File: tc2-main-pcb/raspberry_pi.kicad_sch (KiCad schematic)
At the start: 30 parts, among them J1 Screw_Terminal_01x01, J2 Screw_Terminal_01x01, J4 Raspberry_Pi_2_3, J5 Screw_Terminal_01x01, J6 Screw_Terminal_01x01, J8 Screw_Terminal_01x01, U14 MAX98357AEWL+T, U15 74HC4052, U18 TCA4311ADGKR

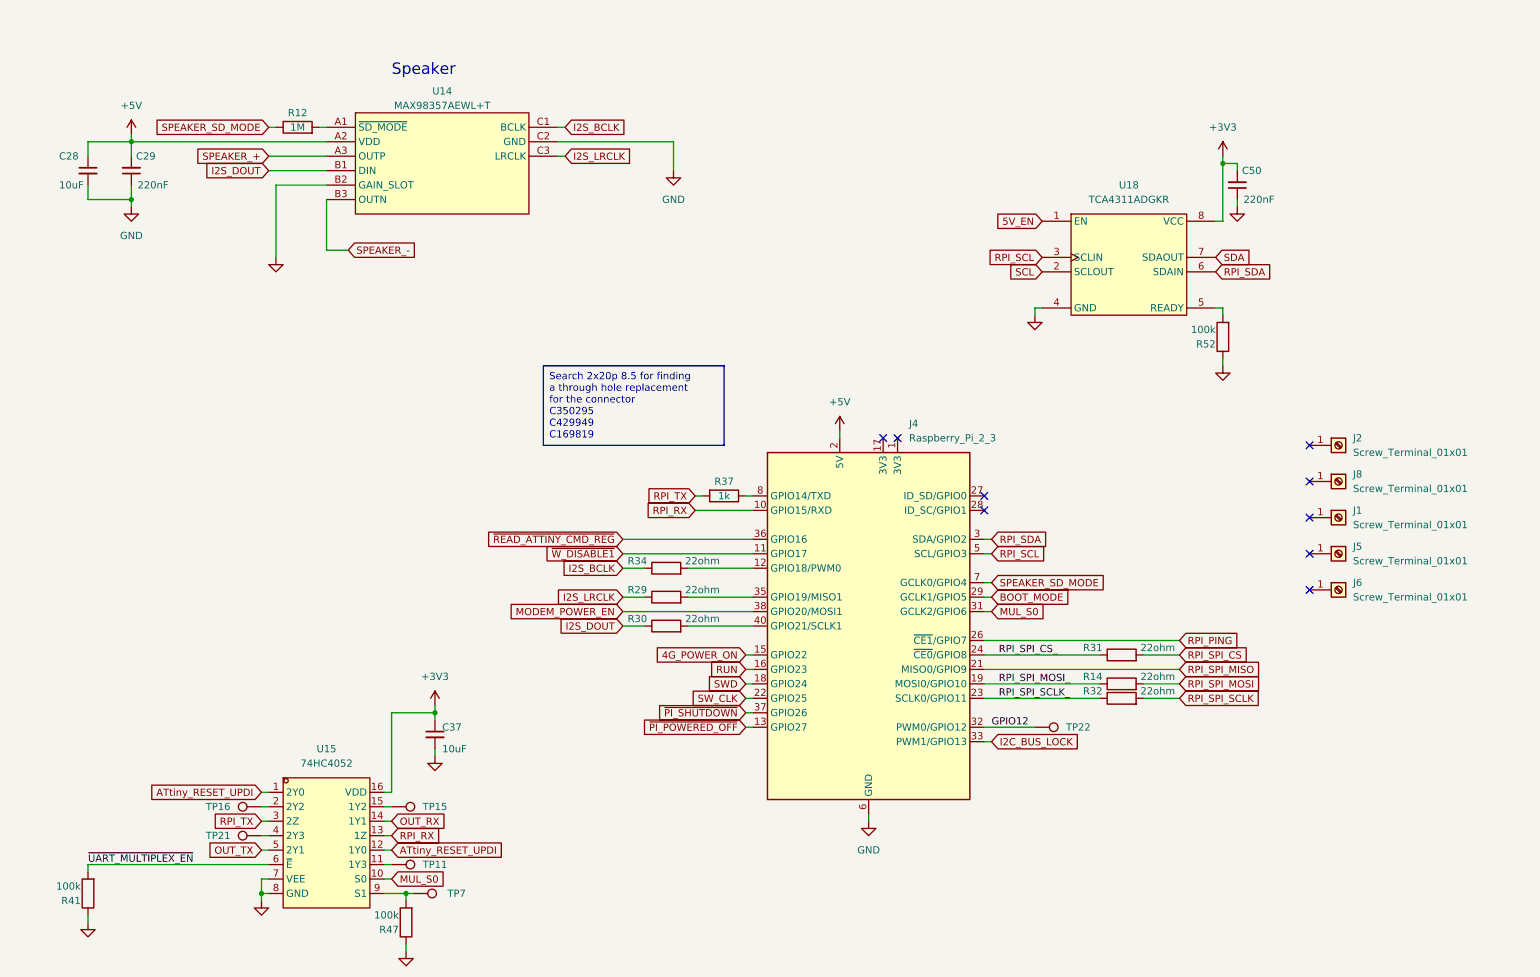
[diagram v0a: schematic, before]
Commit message: Update to use touch sensor
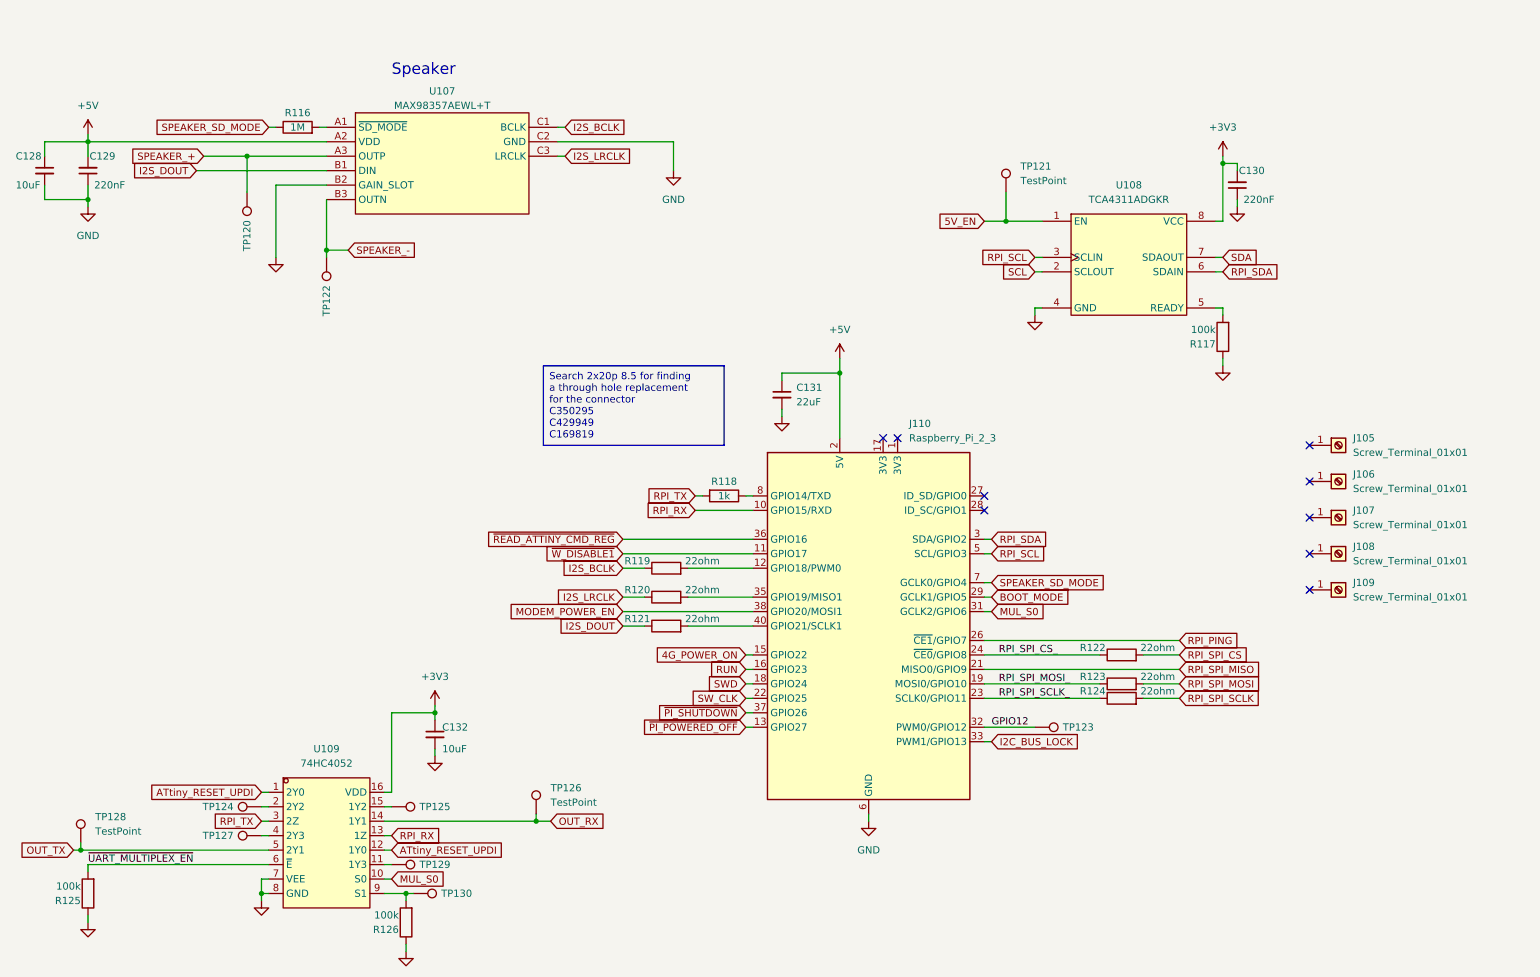
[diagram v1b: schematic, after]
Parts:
- added C131: 22uF, Capacitor_SMD:C_0603_1608Metric, symbol Device:C_Small
- added TP120, TP122: TestPoint, cacophony-library:TP, symbol Connector:TestPoint
- added TP121, TP126, TP128: TestPoint, TestPoint:TestPoint_Pad_D1.0mm, symbol Connector:TestPoint
- J110: renamed from J4; footprint cacophony-library:HDR-SMD_40P-P2.54-V-F-R2-C20-LS8.2-EH -> cacophony-library:rpi-throughhole-socket; LCSC C2685098 -> C350295
- R116: renamed from R12; LCSC C22935 -> C326730
- renumbered C28 to C128, C29 to C129, C50 to C130, C37 to C132, J2 to J105, J8 to J106, J1 to J107, J5 to J108, J6 to J109, R52 to R117, R37 to R118, R34 to R119, R29 to R120, R30 to R121, R31 to R122, R14 to R123, R32 to R124, R41 to R125, R47 to R126, TP22 to TP123, TP16 to TP124, TP15 to TP125, TP21 to TP127, TP11 to TP129, TP7 to TP130, U14 to U107, U18 to U108, U15 to U109
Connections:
- net +5V: now also C131.1
- net 5V_EN: now also TP121.1
- net GND: now also C131.2
- net OUT_RX: now also TP126.1
- net OUT_TX: now also TP128.1
- net SPEAKER_+: now also TP120.1
- net SPEAKER_-: now also TP122.1
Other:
- moved on the sheet: C128, C129

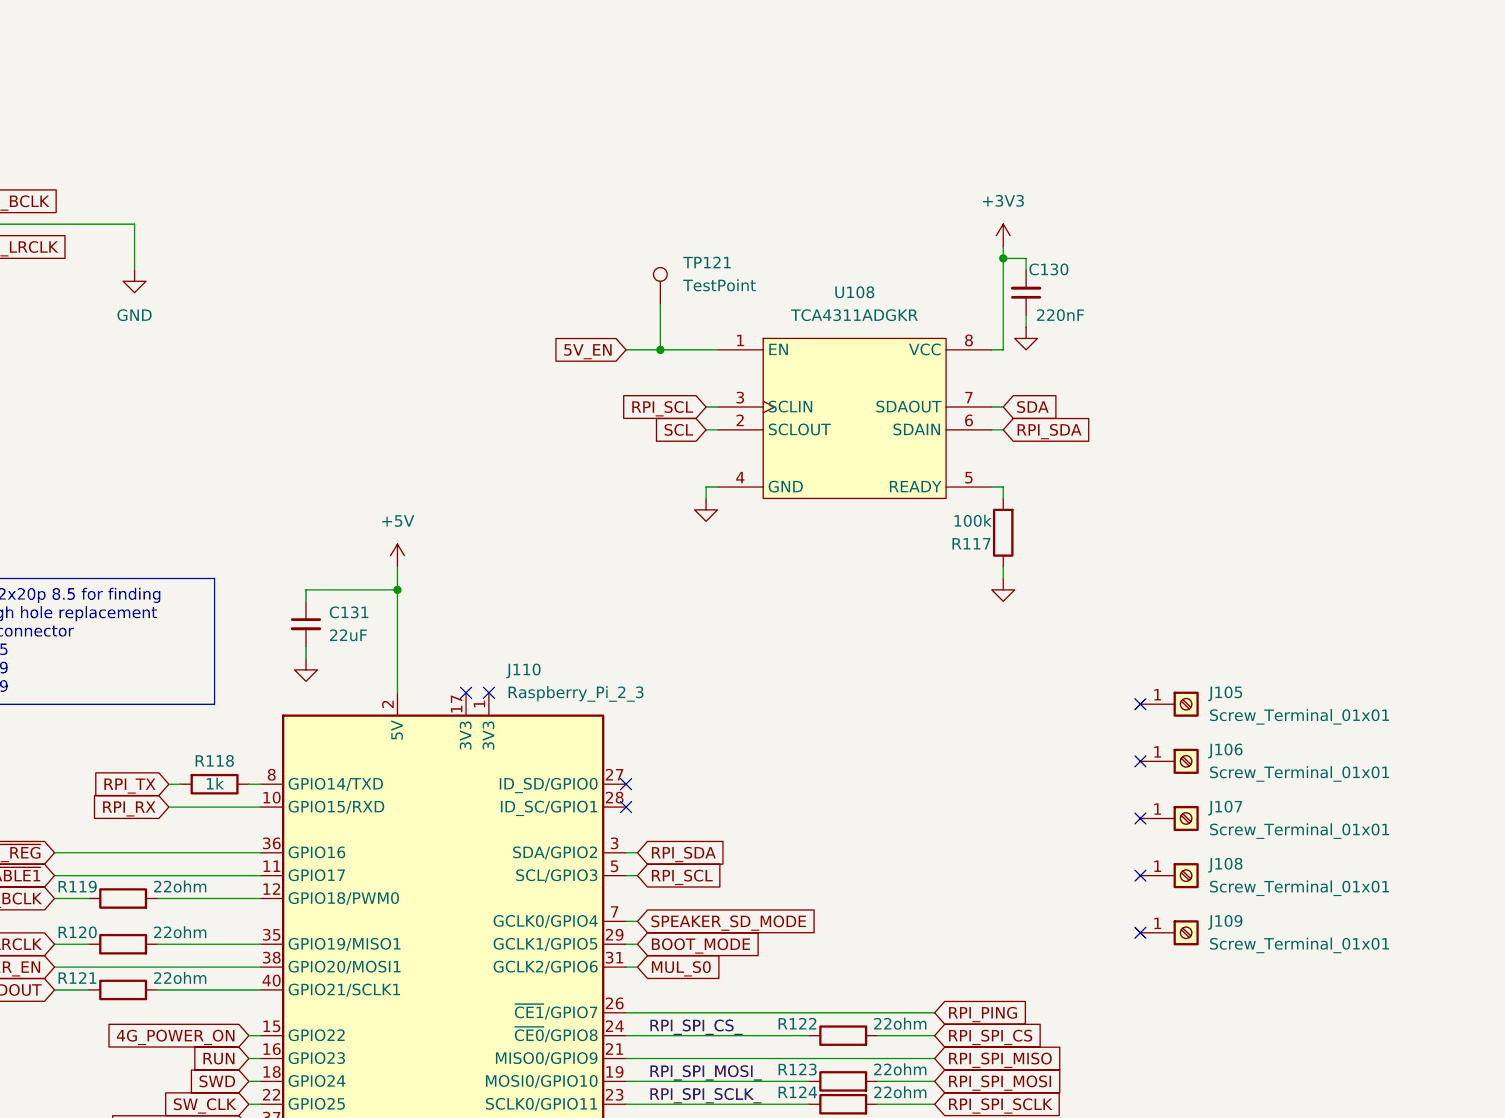
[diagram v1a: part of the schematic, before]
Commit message: Change to through hole connector and add simcard PCB to pannel
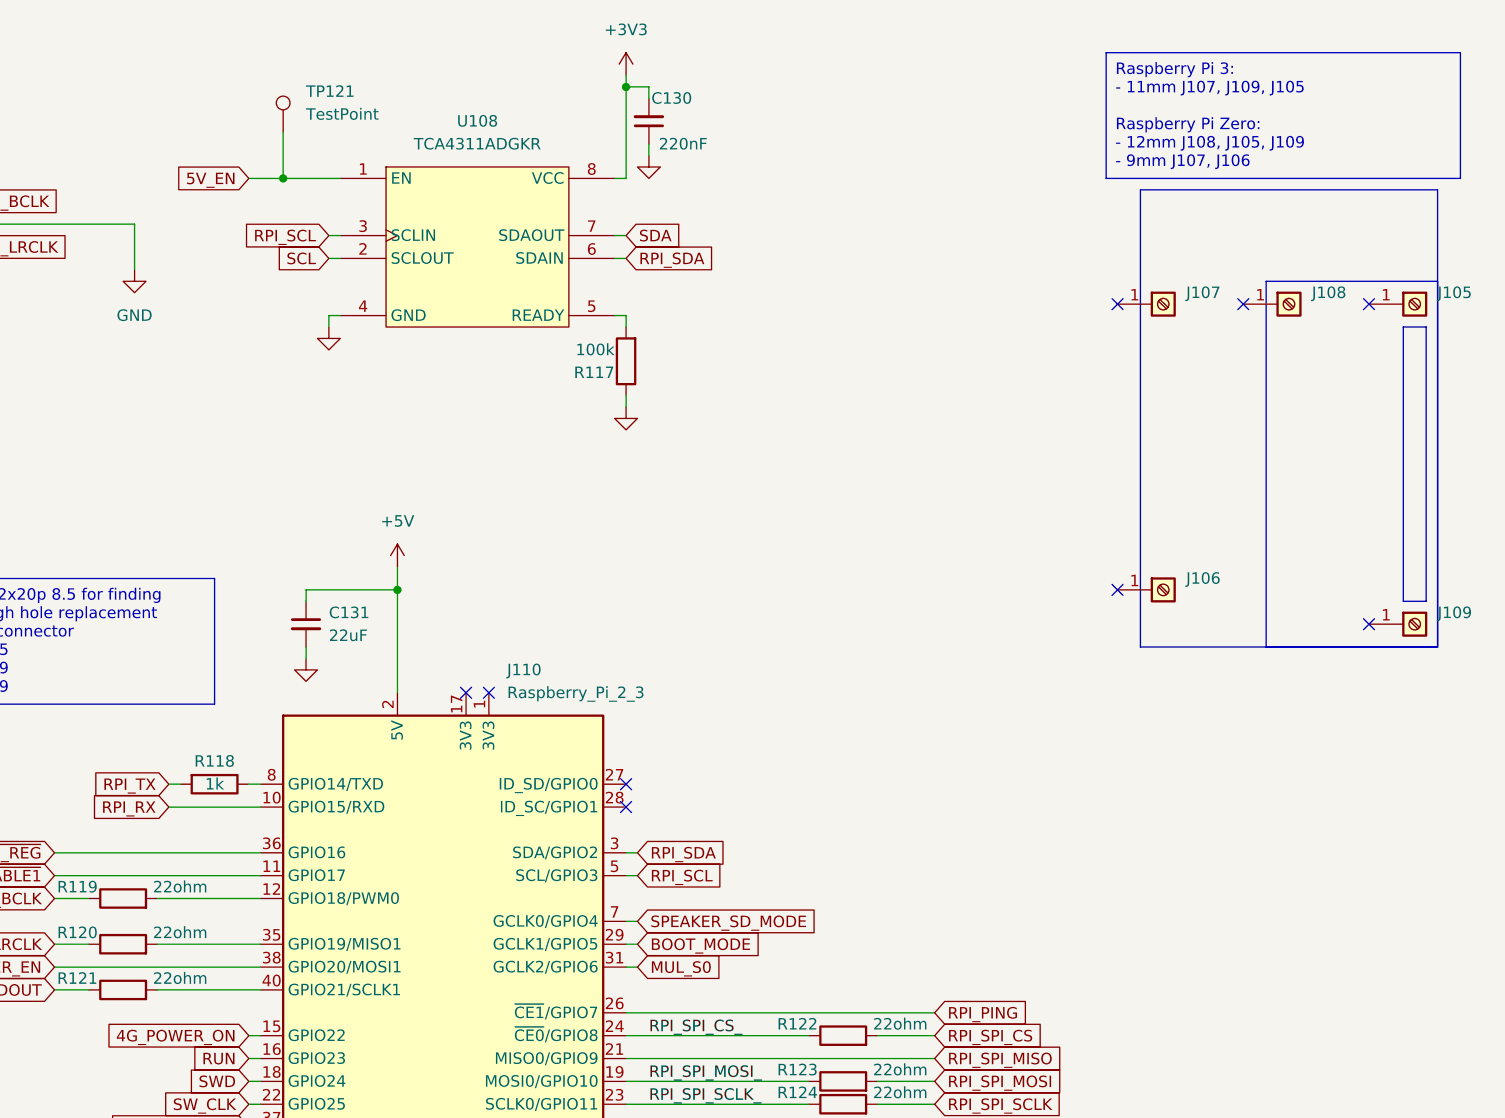
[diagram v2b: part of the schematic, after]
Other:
- moved on the sheet: C130, J105, J106, J107, J108, J109, R117, TP121, U108

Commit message: v0.7.2 panelise microphone boards
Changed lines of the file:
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@@
-		)
-	)
-	(text_box "Search 2x20p 8.5 for finding a through hole replacement for the connector\nC350295\nC429949\nC169819"
-		(exclude_from_sim no)
-		(at 111.76 77.47 0)
-		(size 31.75 13.97)
-		(stroke
-			(width 0)
-			(type default)
-		)
-		(fill
-			(type none)
-		)
-		(effects
-			(font
-				(size 1.27 1.27)
-			)
-			(justify left top)
 		)
 	)

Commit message: 0.8.0 WIP
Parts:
- R119, R120, R121, R122, R123, R124: value 22ohm -> 22Ω
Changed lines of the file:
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@@
 	(label "GPIO12"
 		(at 190.5 140.97 0)
-		(fields_autoplaced yes)
 		(effects
 			(font
@@
 	(label "RPI_SPI_SCLK_"
 		(at 191.77 135.89 0)
-		(fields_autoplaced yes)
 		(effects
 			(font
@@
 	(label "RPI_SPI_CS_"
 		(at 191.77 128.27 0)
-		(fields_autoplaced yes)
 		(effects
 			(font
@@
 	(label "~{UART_MULTIPLEX_EN}"
 		(at 31.75 165.1 0)
-		(fields_autoplaced yes)
 		(effects
 			(font
@@
 	(label "RPI_SPI_MOSI_"
 		(at 191.77 133.35 0)
-		(fields_autoplaced yes)
 		(effects
 			(font
@@
 			)
 		)
-		(property "Value" "22ohm"
+		(property "Value" "22Ω"
 			(at 139.7 121.92 90)
 			(effects
@@
 			)
 		)
-		(property "Value" "22ohm"
+		(property "Value" "22Ω"
 			(at 219.71 132.08 90)
 			(effects
@@
 			)
 		)
-		(property "Value" "22ohm"
+		(property "Value" "22Ω"
 			(at 139.7 116.84 90)
 			(effects
@@
 			)
 		)
-		(property "Value" "22ohm"
+		(property "Value" "22Ω"
 			(at 139.7 111.76 90)
 			(effects
@@
 			)
 		)
-		(property "Value" "22ohm"
+		(property "Value" "22Ω"
 			(at 219.71 127 90)
 			(effects
@@
 			)
 		)
-		(property "Value" "22ohm"
+		(property "Value" "22Ω"
 			(at 219.71 134.62 90)
 			(effects

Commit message: Updated to use field LCSC Part instead of LCSC for the JLCPCB part number
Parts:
- C128, C132: LCSC C19702 -> (none); LCSC Part (none) -> C19702
- C129, C130: LCSC C16772 -> (none); LCSC Part (none) -> C16772
- C131: LCSC C86295 -> (none); LCSC Part (none) -> C86295
- J105, J106, J107, J108, J109: LCSC C2915630 -> (none); LCSC Part (none) -> C2915630
- J110: LCSC C350295 -> (none); LCSC Part (none) -> C350295
- R116: LCSC C326730 -> (none); LCSC Part (none) -> C326730
- R117, R125, R126: LCSC C25741 -> (none); LCSC Part (none) -> C25741
- R118: LCSC C11702 -> (none); LCSC Part (none) -> C11702
- R119, R120, R121, R122, R123, R124: LCSC C25092 -> (none); LCSC Part (none) -> C25092
- U107: LCSC C2682619 -> (none); LCSC Part (none) -> C2682619
- U108: footprint Package_SO:MSOP-8_3x3mm_P0.65mm -> cacophony-library:MSOP-8_L3.0-W3.0-P0.65-LS5.0-BL; LCSC C130025 -> (none); LCSC Part (none) -> C130025
- U109: footprint Package_SO:SOP-16_3.9x9.9mm_P1.27mm -> cacophony-library:SOP-16_L10.0-W3.9-P1.27-LS6.0-BL; LCSC C111594 -> (none); LCSC Part (none) -> C111594
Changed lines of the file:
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@@
 			)
 		)
-		(property "LCSC Part" ""
+		(property "LCSC Part" "C2682619"
 			(at 93.98 60.96 0)
 			(effects
@@
 			)
 		)
-		(property "LCSC" "C2682619 "
+		(property "LCSC Part" "C2682619"
 			(at 93.98 40.64 0)
 			(effects
@@
 			)
 		)
-		(property "LCSC" "C2915630"
+		(property "LCSC Part" "C2915630"
 			(at 276.86 82.55 0)
 			(effects
@@
 			)
 		)
-		(property "LCSC" "C25092"
+		(property "LCSC Part" "C25092"
 			(at 133.35 123.19 0)
 			(effects
@@
 			)
 		)
-		(property "LCSC" "C16772"
+		(property "LCSC Part" "C16772"
 			(at 191.77 26.67 0)
 			(effects
@@
 			)
 		)
-		(property "LCSC" "C25741"
+		(property "LCSC Part" "C25741"
 			(at 189.23 53.34 0)
 			(effects
@@
 			)
 		)
-		(property "LCSC" "C11702"
+		(property "LCSC Part" "C11702"
 			(at 143.51 100.33 0)
 			(effects
@@
 			)
 		)
-		(property "Footprint" "Package_SO:MSOP-8_3x3mm_P0.65mm"
+		(property "Footprint" "cacophony-library:MSOP-8_L3.0-W3.0-P0.65-LS5.0-BL"
 			(at 172.72 54.61 0)
 			(effects
@@
 			)
 		)
-		(property "LCSC Part" ""
+		(property "LCSC Part" "C130025"
 			(at 172.72 59.69 0)
 			(effects
@@
 			)
 		)
-		(property "LCSC" "C130025"
+		(property "LCSC Part" "C130025"
 			(at 172.72 40.64 0)
 			(effects
@@
 			)
 		)
-		(property "LCSC" "C25741"
+		(property "LCSC Part" "C25741"
 			(at 31.75 170.18 0)
 			(effects
@@
 			)
 		)
-		(property "LCSC" "C25092"
+		(property "LCSC Part" "C25092"
 			(at 213.36 133.35 0)
 			(effects
@@
 			)
 		)
-		(property "LCSC" "C2915630"
+		(property "LCSC Part" "C2915630"
 			(at 248.92 78.74 0)
 			(effects
@@
 			)
 		)
-		(property "LCSC" "C326730"
+		(property "LCSC Part" "C326730"
 			(at 68.58 35.56 90)
 			(effects
@@
 			)
 		)
-		(property "LCSC" "C86295"
+		(property "LCSC Part" "C86295"
 			(at 153.67 82.55 0)
 			(effects
@@
 			)
 		)
-		(property "LCSC" "C2915630"
+		(property "LCSC Part" "C2915630"
 			(at 276.86 46.99 0)
 			(effects
@@
 			)
 		)
-		(property "LCSC" "C25092"
+		(property "LCSC Part" "C25092"
 			(at 133.35 118.11 0)
 			(effects
@@
 			)
 		)
-		(property "LCSC" "C19702"
+		(property "LCSC Part" "C19702"
 			(at 24.13 43.18 0)
 			(effects
@@
 			)
 		)
-		(property "LCSC" "C2915630"
+		(property "LCSC Part" "C2915630"
 			(at 262.89 46.99 0)
 			(effects
@@
 			)
 		)
-		(property "LCSC" "C350295"
+		(property "LCSC Part" "C350295"
 			(at 168.91 123.19 0)
 			(effects
@@
 			)
 		)
-		(property "LCSC" "C16772"
+		(property "LCSC Part" "C16772"
 			(at 31.75 43.18 0)
 			(effects
@@
 			)
 		)
-		(property "LCSC" "C25092"
+		(property "LCSC Part" "C25092"
 			(at 133.35 113.03 0)
 			(effects
@@
 			)
 		)
-		(property "LCSC" "C25092"
+		(property "LCSC Part" "C25092"
 			(at 213.36 128.27 0)
 			(effects
@@
 			)
 		)
-		(property "LCSC" "C19702"
+		(property "LCSC Part" "C19702"
 			(at 92.71 142.24 0)
 			(effects
@@
 			)
 		)
-		(property "LCSC" "C25741"
+		(property "LCSC Part" "C25741"
 			(at 87.63 175.26 0)
 			(effects
@@
 			)
 		)
-		(property "Footprint" "Package_SO:SOP-16_3.9x9.9mm_P1.27mm"
+		(property "Footprint" "cacophony-library:SOP-16_L10.0-W3.9-P1.27-LS6.0-BL"
 			(at 73.66 177.8 0)
 			(effects
@@
 			)
 		)
-		(property "LCSC Part" ""
+		(property "LCSC Part" "C111594"
 			(at 73.66 182.88 0)
 			(effects
@@
 			)
 		)
-		(property "LCSC" "C111594"
+		(property "LCSC Part" "C111594"
 			(at 73.66 161.29 0)
 			(effects
@@
 			)
 		)
-		(property "LCSC" "C25092"
+		(property "LCSC Part" "C25092"
 			(at 213.36 135.89 0)
 			(effects
@@
 			)
 		)
-		(property "LCSC" "C2915630"
+		(property "LCSC Part" "C2915630"
 			(at 248.92 46.99 0)
 			(effects

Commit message: Tidy up
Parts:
- J110: footprint cacophony-library:rpi-throughhole-socket -> cacophony-library:rpi-zero-throughhole-socket
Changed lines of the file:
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@@
 			)
 		)
-		(property "Footprint" "cacophony-library:rpi-throughhole-socket"
+		(property "Footprint" "cacophony-library:rpi-zero-throughhole-socket"
 			(at 168.91 123.19 0)
 			(effects

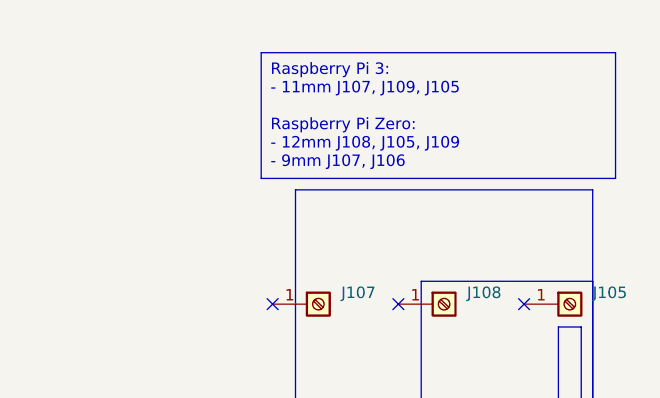
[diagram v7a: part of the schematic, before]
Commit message: Update to kicad 9, fix microphone panel v cuts
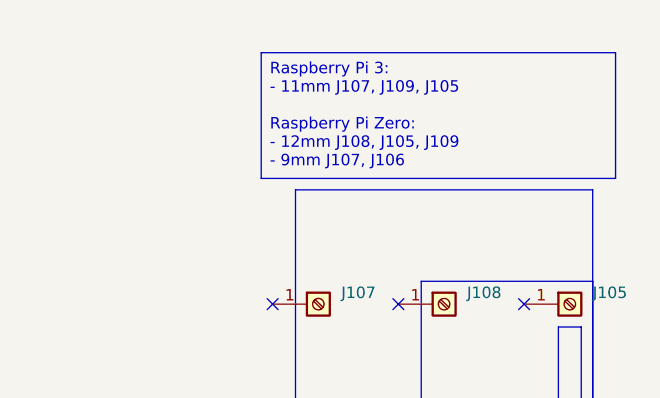
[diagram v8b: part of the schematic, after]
